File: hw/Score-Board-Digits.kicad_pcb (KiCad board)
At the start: 2 copper layers, 32 parts, among them J1 Conn_02x09_Odd_Even

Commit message: PCB routed v1
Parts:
- moved OPT10 38.6 mm to (29.2, 122.0)
- moved OPT1 38.6 mm to (29.2, 134.7)
- moved OPT-IND1 31.0 mm to (28.0, 147.4)
- moved H3 12.7 mm to (26.7, 200.7)
- moved H4 12.7 mm to (191.8, 200.7)
- moved LED1 6.35 mm to (52.1, 194.4)
- moved LED2 6.35 mm to (90.2, 194.4)
- moved LED3 6.35 mm to (128.3, 194.4)
- moved LED4 6.35 mm to (166.4, 194.4)
- moved R1 0.23 mm to (86.4, 120.5)
- moved R2 0.23 mm to (91.5, 120.5)
- moved R3 0.23 mm to (96.5, 120.5)
- moved R4 0.23 mm to (101.6, 120.5)
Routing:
- net /SDA.P: track 0.00 -> 396.3 mm
- net /SDA.G: track 0.00 -> 358.9 mm
- net Net-(OPT1-Pin_2): track 0.00 -> 348.3 mm
- net /SDA.D: track 0.00 -> 315.6 mm
- net /SDA.F: track 0.00 -> 280.8 mm
- net /SDA.C: track 0.00 -> 280.4 mm
- net Net-(OPT10-Pin_2): track 0.00 -> 257.7 mm
- net /SDA.E: track 0.00 -> 232.0 mm
- net Net-(LED1-A): track 0.00 -> 205.0 mm
- net /SDA.A: track 0.00 -> 198.6 mm
- net /SDA.B: track 0.00 -> 182.2 mm
- net Net-(LED4-K): track 0.00 -> 116.6 mm
- net /SD.P: track 0.00 -> 114.3 mm
- net /SD.G: track 0.00 -> 106.3 mm
- net /SD.F: track 0.00 -> 98.6 mm
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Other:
- board outline added: 190.5 x 190.5 mm

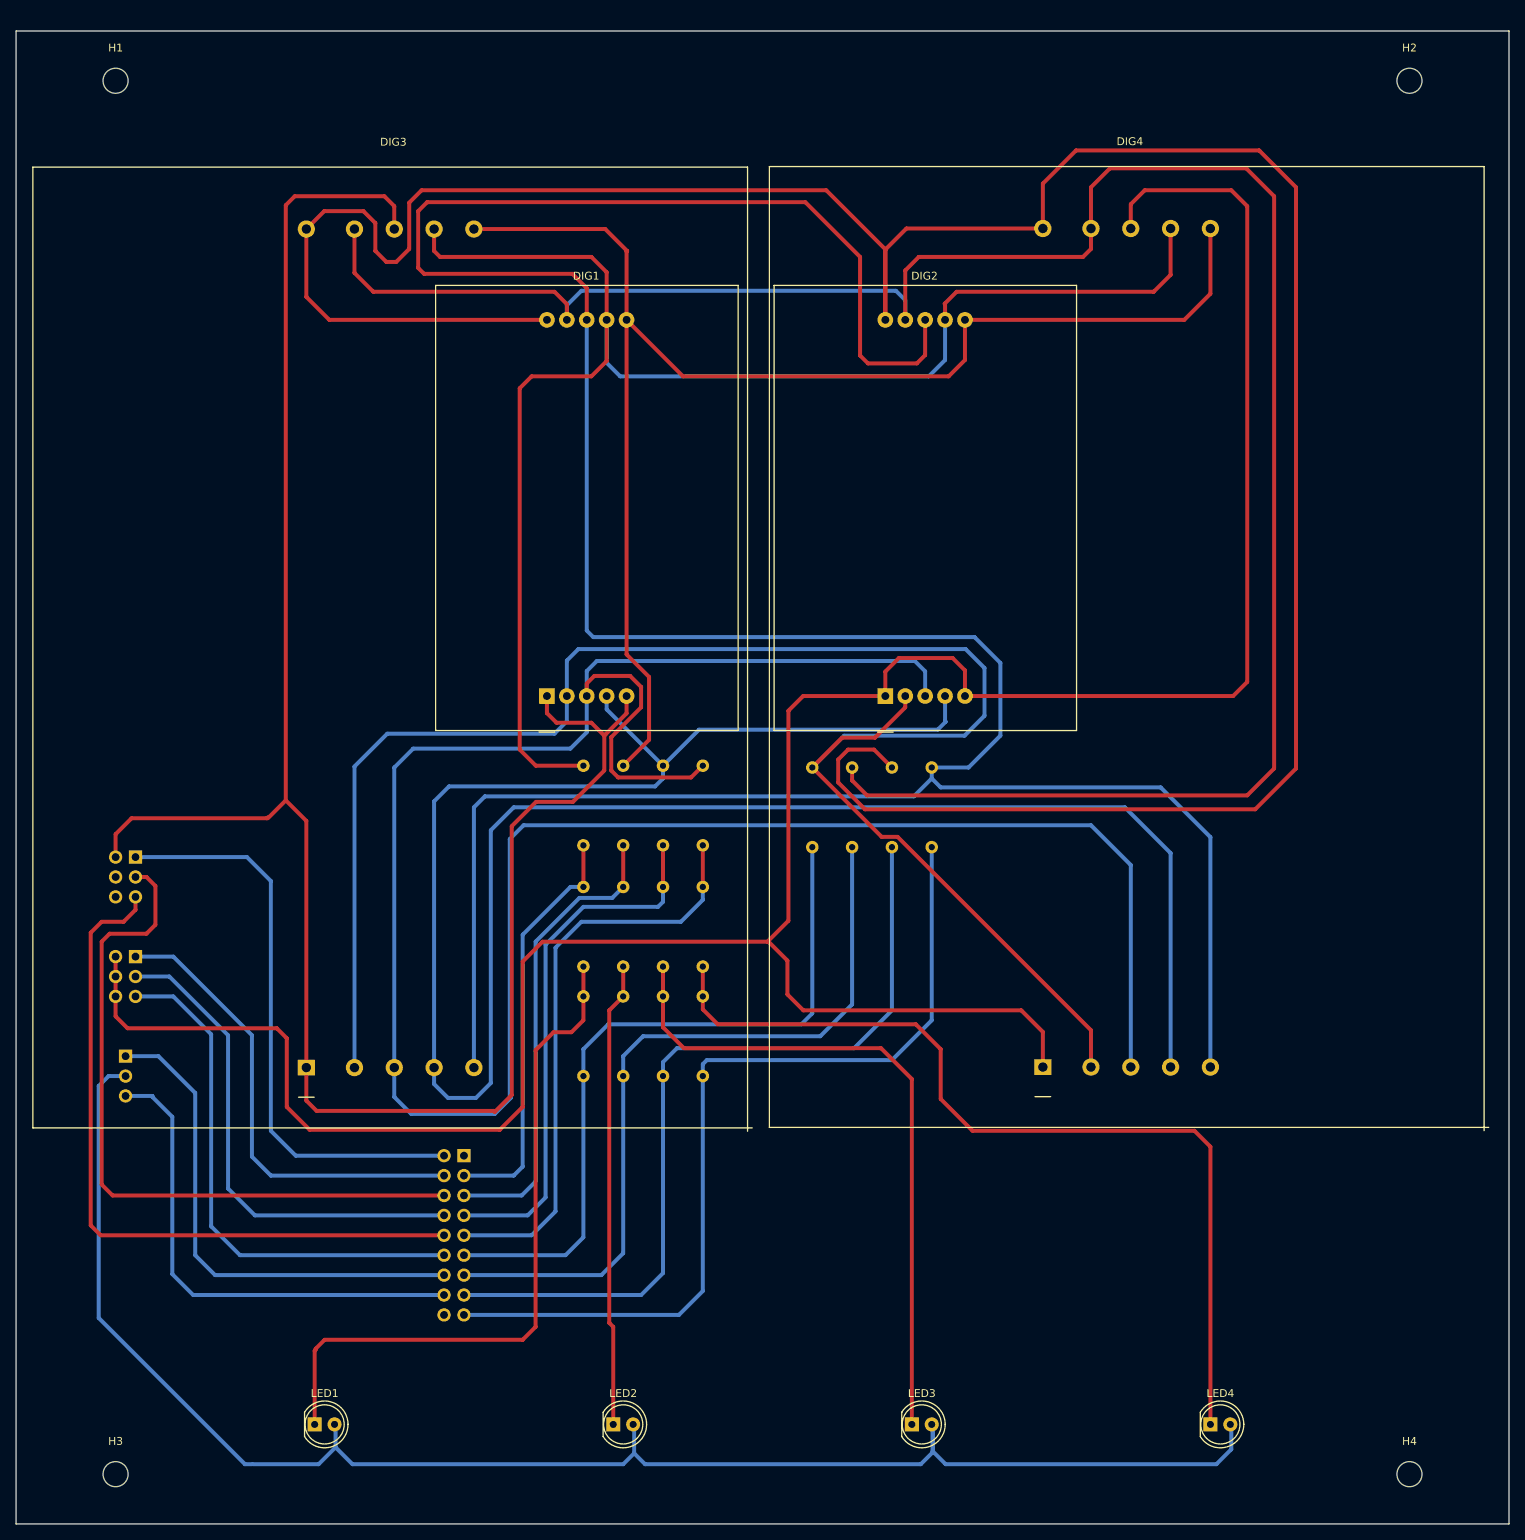
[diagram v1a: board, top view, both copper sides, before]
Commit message: Main schematic ready for board layout
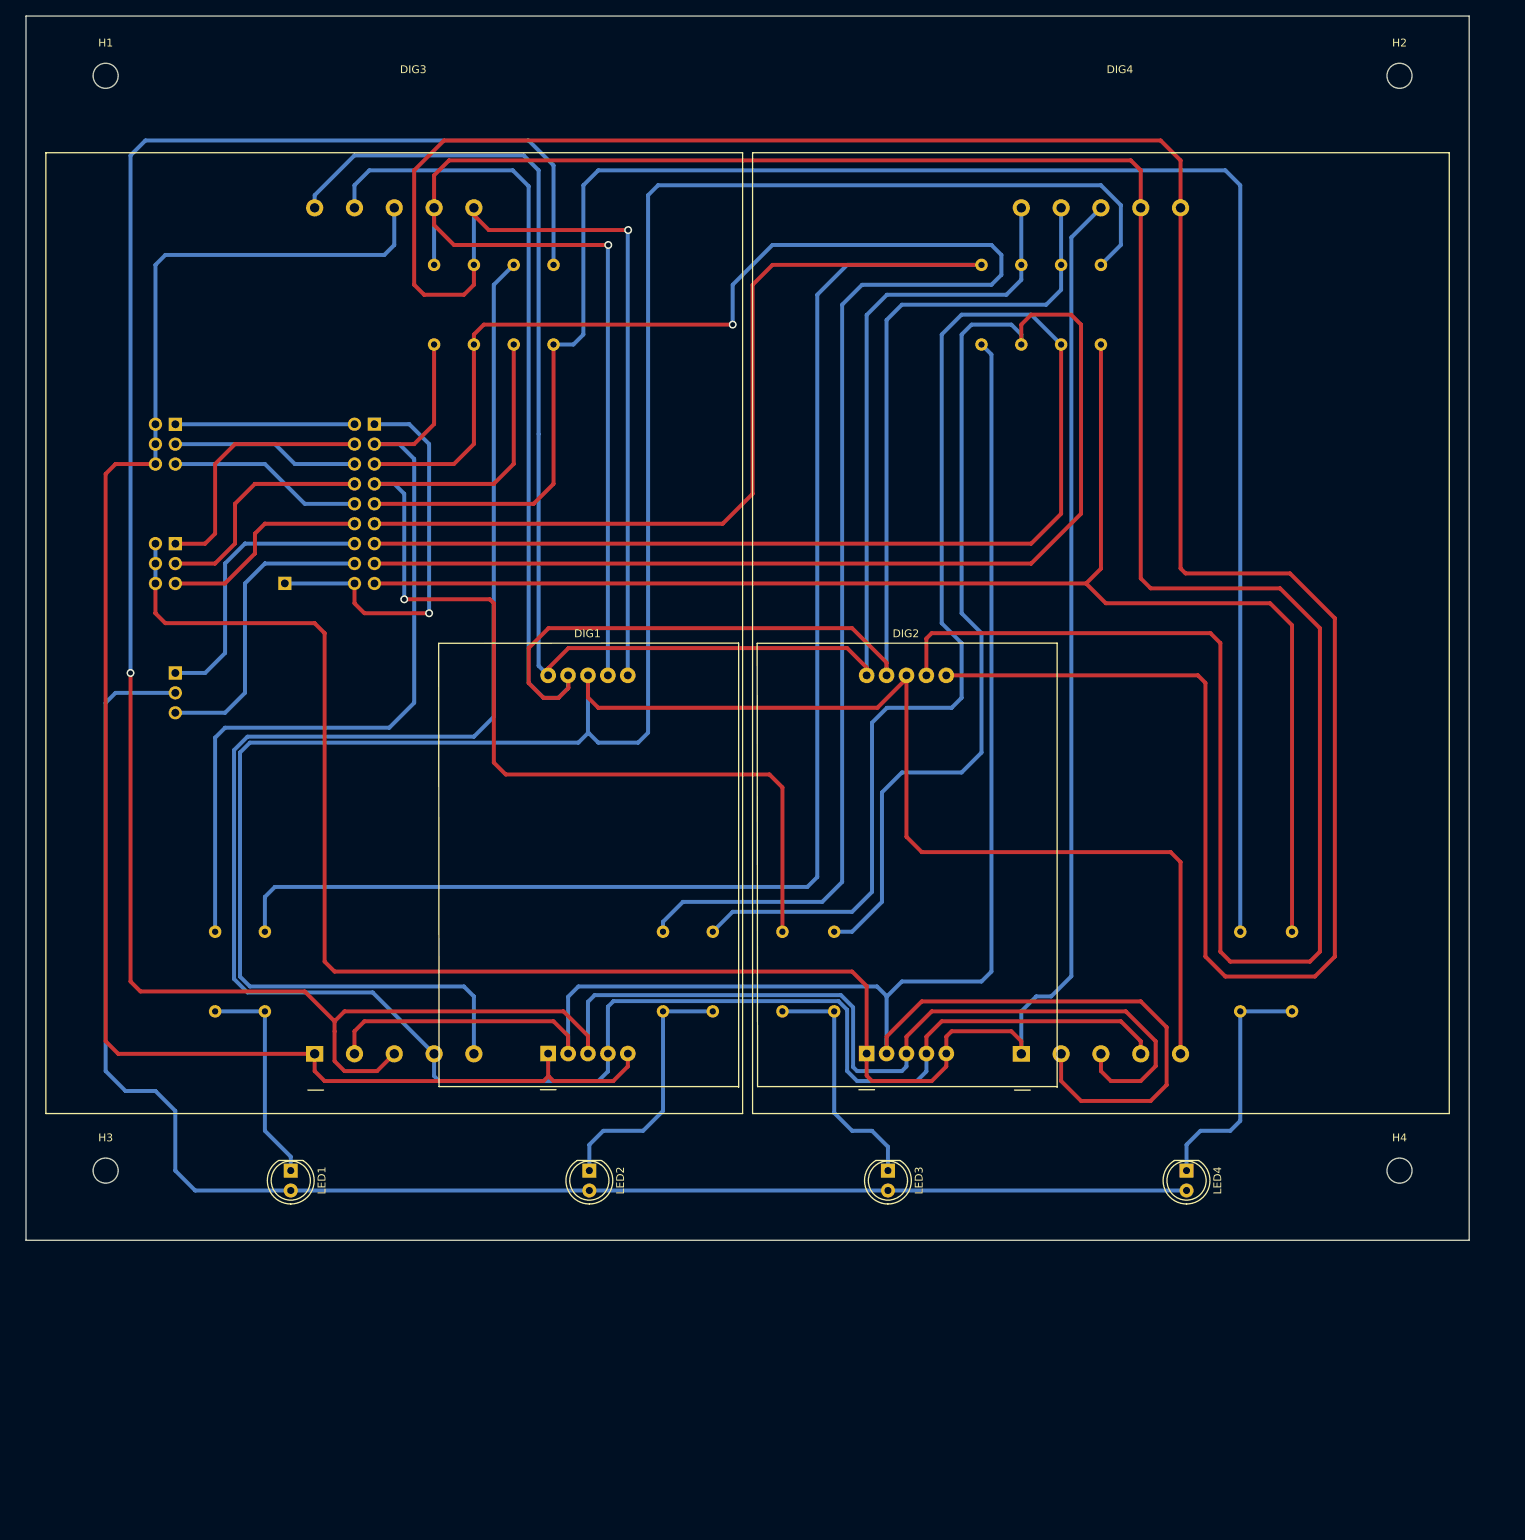
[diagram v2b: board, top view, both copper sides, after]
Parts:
- added GND1: Conn_01x01, Connector_PinHeader_2.54mm:PinHeader_1x01_P2.54mm_Vertical, B.Cu at (48.3, 87.1)
- moved J1 94.0 mm to (59.7, 66.8)
- moved R16 77.4 mm to (176.8, 131.5), turned to -90 degrees
- moved R5 77.4 mm to (137.2, 46.4), turned to -90 degrees
- moved R6 69.5 mm to (147.3, 56.6)
- moved R12 68.8 mm to (170.2, 131.5)
- moved R8 67.7 mm to (152.4, 56.6)
- moved R1 66.7 mm to (67.3, 56.6)
- moved R2 66.7 mm to (72.4, 56.6)
- moved R3 66.7 mm to (77.5, 56.6)
- moved R4 66.7 mm to (82.6, 56.6)
- moved R7 66.2 mm to (142.3, 56.6)
- moved OPT10 55.5 mm to (34.3, 66.8)
- moved OPT1 52.9 mm to (34.3, 82.0)
- moved OPT-IND1 49.3 mm to (34.3, 98.5)
- moved R9 47.3 mm to (39.4, 131.5)
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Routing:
- net /SDA.B: track 182.2 -> 416.3 mm, vias 0 -> 1
- net /SDA.A: track 198.6 -> 398.3 mm, vias 0 -> 1
- net /SD.E: track 92.5 -> 279.6 mm
- net /SD.D: track 74.9 -> 245.7 mm
- net /SD.B: track 59.9 -> 227.6 mm, vias 0 -> 1
- net /SDA.G: track 358.9 -> 219.4 mm
- net /SD.F: track 98.6 -> 232.8 mm
- net /SD.G: track 106.3 -> 228.9 mm
- net Net-(LED4-K): track 116.6 -> 32.0 mm
- net /SD.P: track 114.3 -> 189.7 mm
- net /SD.C: track 68.1 -> 140.4 mm, vias 0 -> 1
- net Net-(J1-Pin_6): track 91.0 -> 23.9 mm
- net Net-(J1-Pin_10): track 91.5 -> 25.0 mm
- net Net-(LED1-K): track 88.8 -> 28.0 mm
- net Net-(LED3-K): track 86.3 -> 31.3 mm
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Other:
- board size 190.5 x 190.5 mm -> 184.1 x 156.2 mm

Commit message: PCB routing done
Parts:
- R1, R2, R3, R4, R5, R6, R7: value 0 -> 77
- R10, R11, R12, R13, R14, R15, R16, R9: value 150 -> 100
- R8: value 0 -> 100
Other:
- board size 184.1 x 156.2 mm -> 184.1 x 152.4 mm

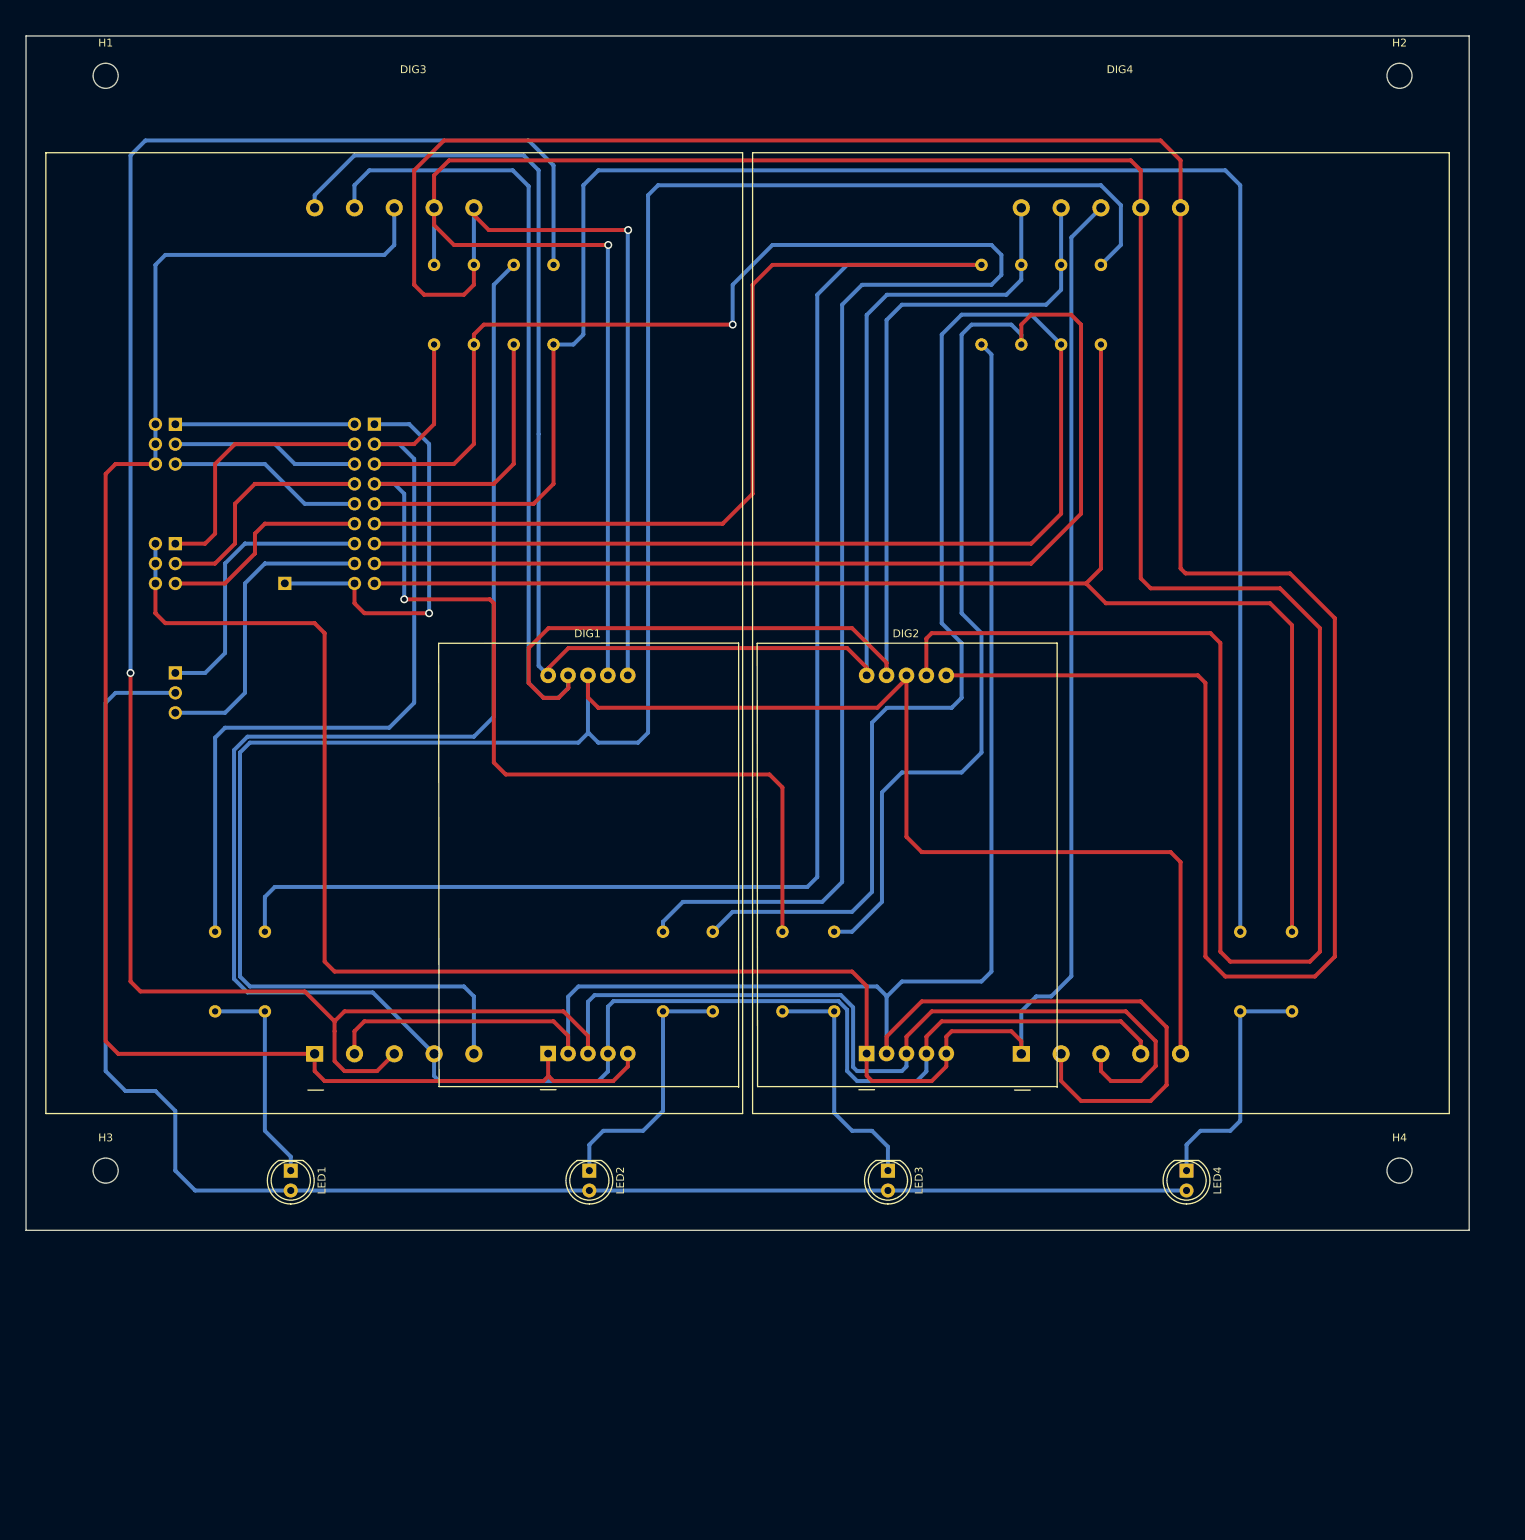
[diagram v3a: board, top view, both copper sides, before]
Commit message: Add pull-down res to segment drives.
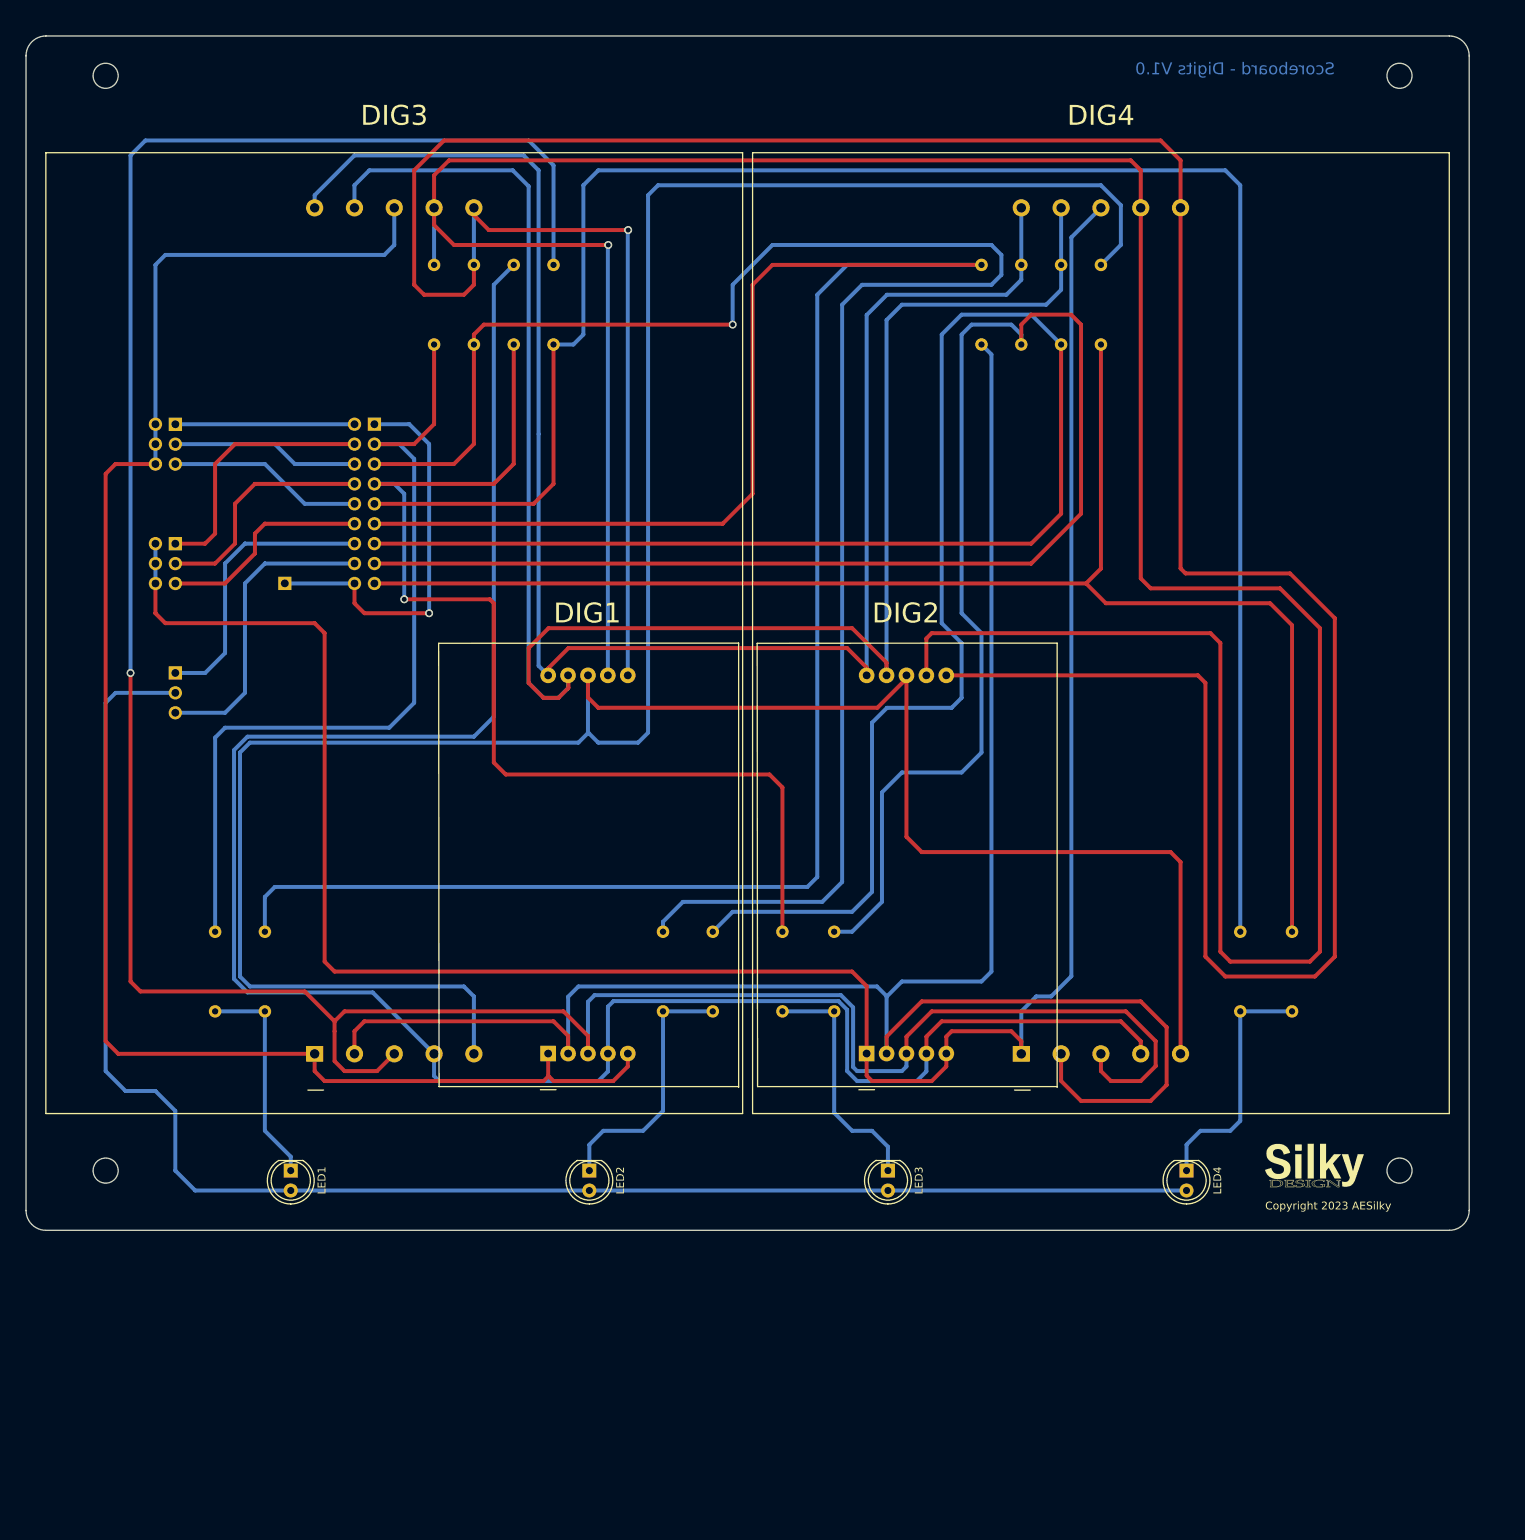
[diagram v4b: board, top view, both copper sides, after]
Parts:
- added G***: LOGO, AES_Library:SILKY-DESIGN-logo-0_50-AES, F.Cu at (179.7, 161.4)
- added G***: LOGO, AES_Library:SILKY-DESIGN-logo-0_50-AES, B.Cu at (179.7, 161.4)
- renumbered GND1 to GND, OPT-IND1 to OPT-IND
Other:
- outline, holes or cut-outs redrawn
- board text added: "Copyright 2023 AESilky"
- board text added: "Scoreboard - Digits V1.0"
